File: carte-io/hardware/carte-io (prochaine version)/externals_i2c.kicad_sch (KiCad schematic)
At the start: 40 parts, among them J10 JST_PH_B4B, J11 JST_PH_B4B, J12 JST_PH_B4B, J13 JST_PH_B4B, J14 JST_PH_B4B, J15 JST_PH_B4B, J16 JST_PH_B4B, J17 JST_PH_B4B, J23 JST_PH_B4B, J24 JST_PH_B4B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

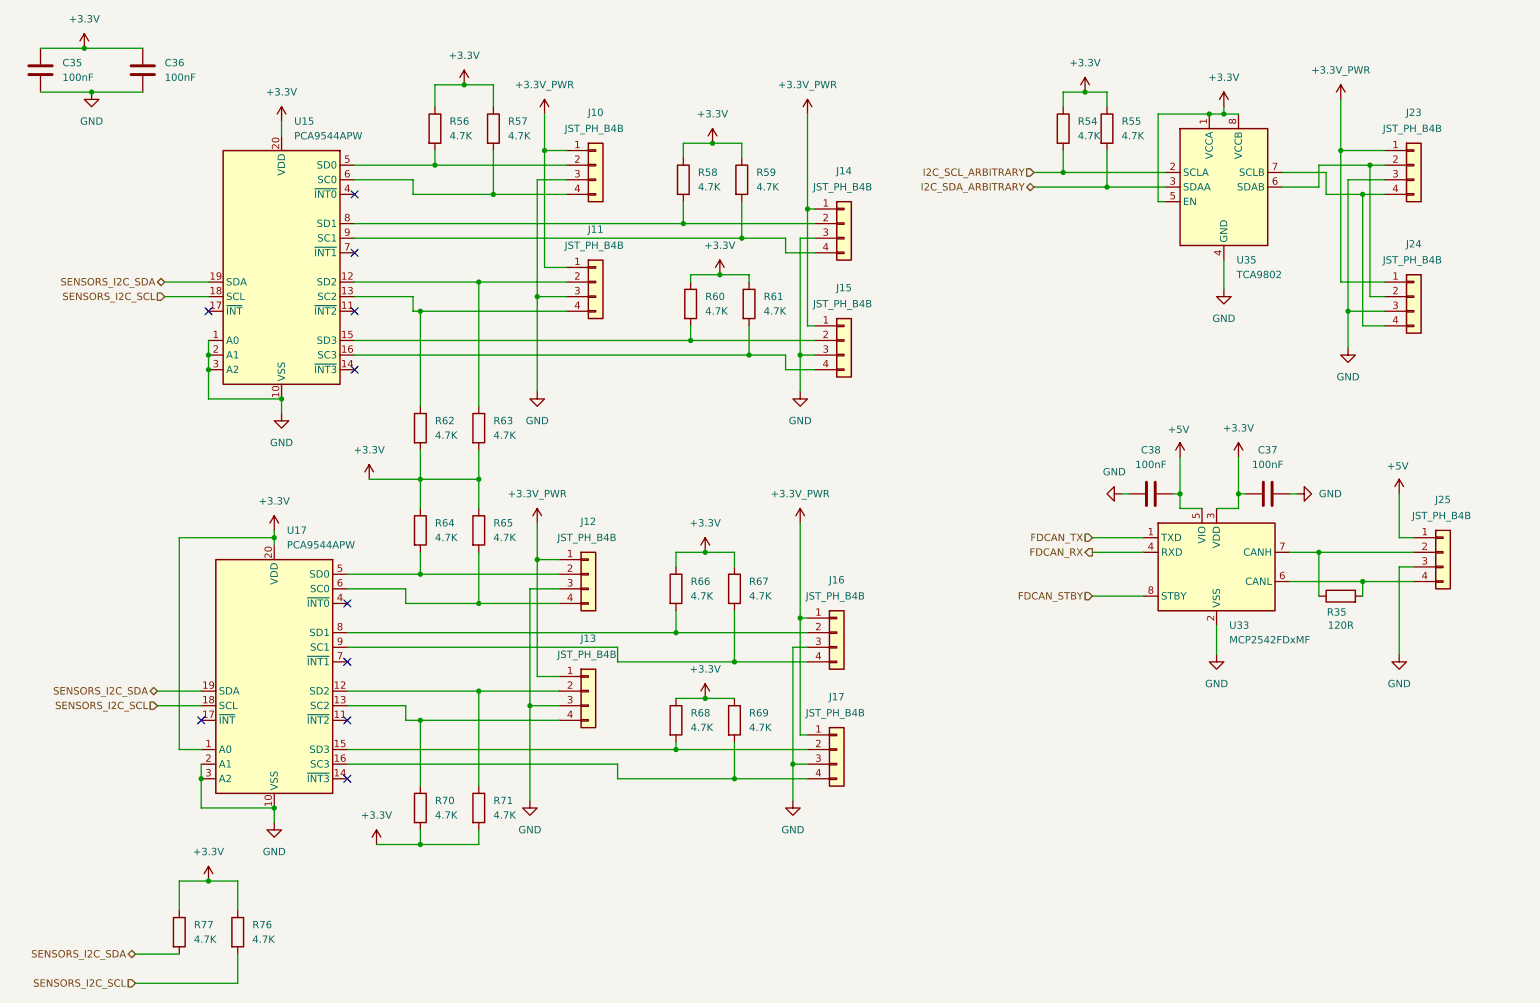
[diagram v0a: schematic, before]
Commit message: Commit de sauvegarde, gros changement sur la carte IO, les connecteurs sont compatibles SeeedStudio Grove. Il faut reprendre une grosse partie du routage et rajouter deux entrées analogiques
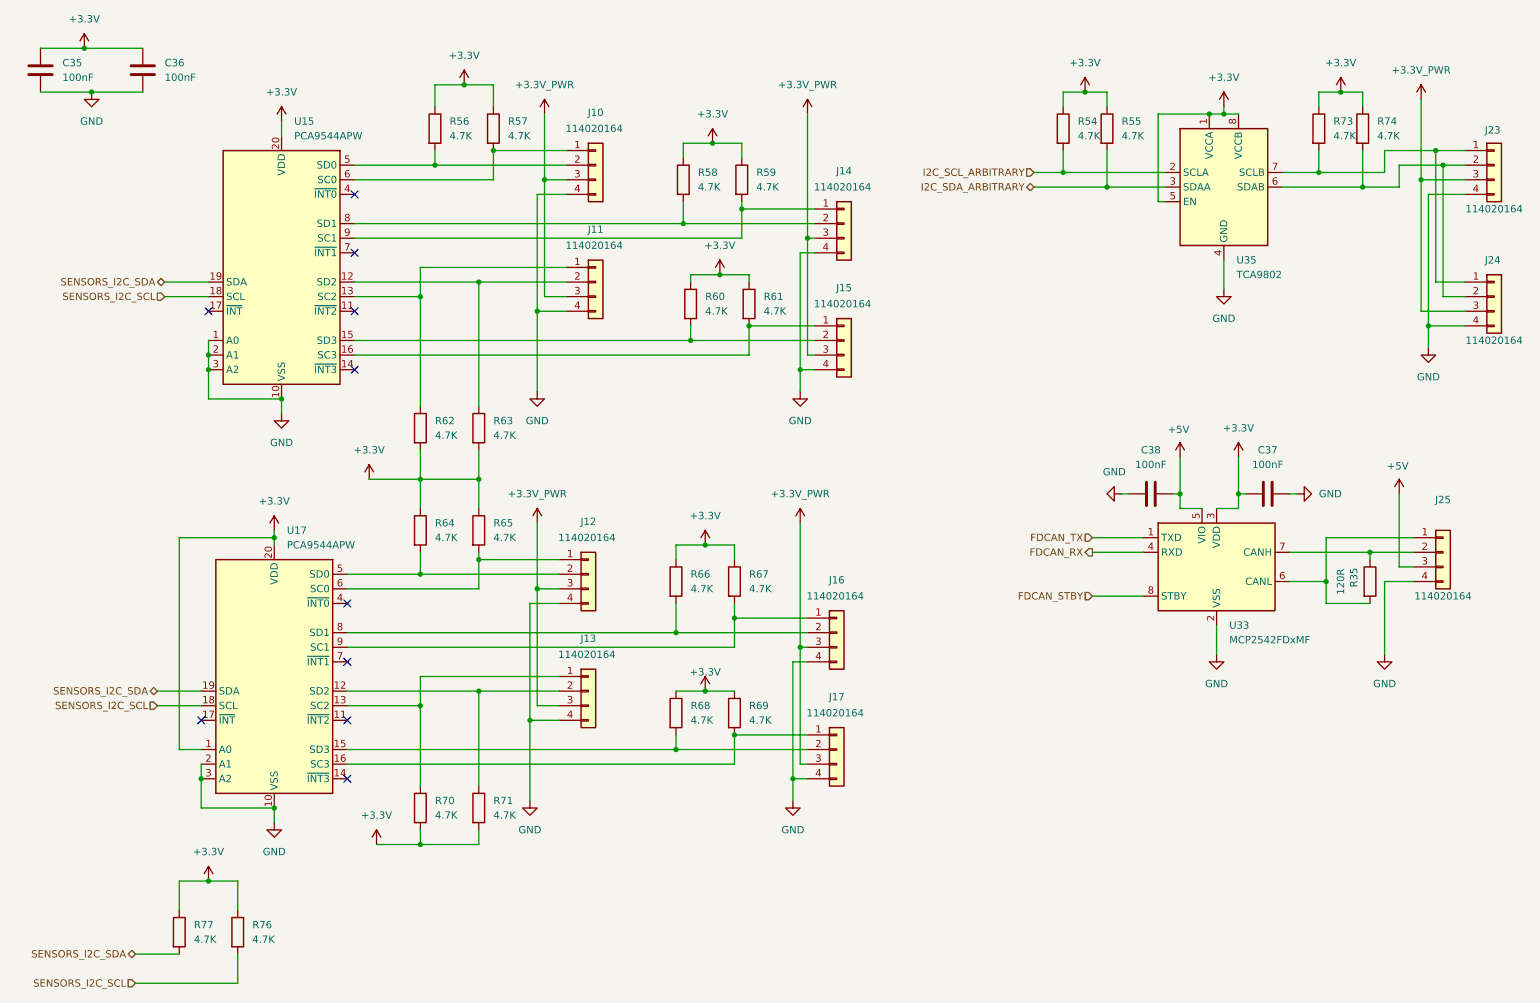
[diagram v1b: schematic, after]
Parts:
- added R73, R74: 4.7K, Resistor_SMD:R_0805_2012Metric_Pad1.20x1.40mm_HandSolder, symbol Device:R
- J10, J11, J12, J13, J14, J15, J16, J17, J23, J24, J25: value JST_PH_B4B -> 114020164; footprint Connector_JST:JST_PH_B4B-PH-K_1x04_P2.00mm_Vertical -> SeeedStudio - Horizontal Header -114020164:SEEEDSTUDIO_114020164; symbol Connector_Generic:Conn_01x04 -> SeeedStudio - Horizontal header:SeeedStudio - 114020164 - R/A
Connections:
- net +3.3V: now also R73.1, R74.1
- net +3.3V_PWR: now also J10.3 (Pin_3), J11.3 (Pin_3), J12.3 (Pin_3), J13.3 (Pin_3), J14.3 (Pin_3), J15.3 (Pin_3), J16.3 (Pin_3), J17.3 (Pin_3), J23.3 (Pin_3), J24.3 (Pin_3); no longer J10.1 (Pin_1), J11.1 (Pin_1), J12.1 (Pin_1), J13.1 (Pin_1), J14.1 (Pin_1), J15.1 (Pin_1), J16.1 (Pin_1), J17.1 (Pin_1), J23.1 (Pin_1), J24.1 (Pin_1)
- net +5V: now also J25.3 (Pin_3); no longer J25.1 (Pin_1)
- net GND: now also J10.4 (Pin_4), J11.4 (Pin_4), J12.4 (Pin_4), J13.4 (Pin_4), J14.4 (Pin_4), J15.4 (Pin_4), J16.4 (Pin_4), J17.4 (Pin_4), J23.4 (Pin_4), J24.4 (Pin_4), J25.4 (Pin_4); no longer J10.3 (Pin_3), J11.3 (Pin_3), J12.3 (Pin_3), J13.3 (Pin_3), J14.3 (Pin_3), J15.3 (Pin_3), J16.3 (Pin_3), J17.3 (Pin_3), J23.3 (Pin_3), J24.3 (Pin_3), J25.3 (Pin_3)
- net at R67.2, U17.9 (SC1): now also J16.1 (Pin_1); no longer J16.4 (Pin_4)
- net at J23.2 (Pin_2), J24.2 (Pin_2), U35.6 (SDAB): now also R74.2
- net at R61.2, U15.16 (SC3): now also J15.1 (Pin_1); no longer J15.4 (Pin_4)
- net at R57.2, U15.6 (SC0): now also J10.1 (Pin_1); no longer J10.4 (Pin_4)
- net at R69.2, U17.16 (SC3): now also J17.1 (Pin_1); no longer J17.4 (Pin_4)
- net at R70.1, U17.13 (SC2): now also J13.1 (Pin_1); no longer J13.4 (Pin_4)
- net at R65.2, U17.6 (SC0): now also J12.1 (Pin_1); no longer J12.4 (Pin_4)
- net at R35.2, U33.6 (CANL): now also J25.1 (Pin_1); no longer J25.4 (Pin_4)
- net at R59.2, U15.9 (SC1): now also J14.1 (Pin_1); no longer J14.4 (Pin_4)
- net at R62.1, U15.13 (SC2): now also J11.1 (Pin_1); no longer J11.4 (Pin_4)
- new net: J23.1 (Pin_1), J24.1 (Pin_1), R73.2, U35.7 (SCLB)
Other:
- moved on the sheet: J23, J24, R35, R66, R67, R68, R69

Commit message: -- reorganisation de la carte, - rajout des connecteurs seeedstudio grove - Rajout des deux entrées ADC
travail en cours
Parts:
- renumbered J14 to J12, J15 to J13, J12 to J14, J13 to J15
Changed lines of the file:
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@@
 		(on_board yes)
 		(dnp no)
-		(property "Reference" "J15"
+		(property "Reference" "J13"
 			(at 165.1 65.786 0)
 			(effects
@@
 			(project "carte-io"
 				(path "/acbeee85-bee7-482c-b859-0ad6bf15d6be/b1447454-b4c9-4241-a4de-131fa2452240"
-					(reference "J15")
+					(reference "J13")
 					(unit 1)
 				)
@@
 		(on_board yes)
 		(dnp no)
-		(property "Reference" "J13"
+		(property "Reference" "J15"
 			(at 120.65 126.746 0)
 			(effects
@@
 			(project "carte-io"
 				(path "/acbeee85-bee7-482c-b859-0ad6bf15d6be/b1447454-b4c9-4241-a4de-131fa2452240"
-					(reference "J13")
+					(reference "J15")
 					(unit 1)
 				)
@@
 		(on_board yes)
 		(dnp no)
-		(property "Reference" "J14"
+		(property "Reference" "J12"
 			(at 165.1 45.466 0)
 			(effects
@@
 			(project "carte-io"
 				(path "/acbeee85-bee7-482c-b859-0ad6bf15d6be/b1447454-b4c9-4241-a4de-131fa2452240"
-					(reference "J14")
+					(reference "J12")
 					(unit 1)
 				)
@@
 		(on_board yes)
 		(dnp no)
-		(property "Reference" "J12"
+		(property "Reference" "J14"
 			(at 120.65 106.426 0)
 			(effects
@@
 			(project "carte-io"
 				(path "/acbeee85-bee7-482c-b859-0ad6bf15d6be/b1447454-b4c9-4241-a4de-131fa2452240"
-					(reference "J12")
-					(unit 1)
-				)
+					(reference "J14")
+					(unit 1)
+				)
